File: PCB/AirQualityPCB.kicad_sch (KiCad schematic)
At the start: 28 parts, among them J1 USB_C_Receptacle_USB2.0_16P, J10 SMA-J-P-H-ST-EM1, J2 TestPoint 5V, J3 TestPoint GND, J4 TestPoint 3.3V, U1 Regulator, U13 ESP32-C3-WROOM-02, U2 USBLC6-2SC6, U3 PTS526 SK15 SMTR2 LFS, U4 RFM95WCW

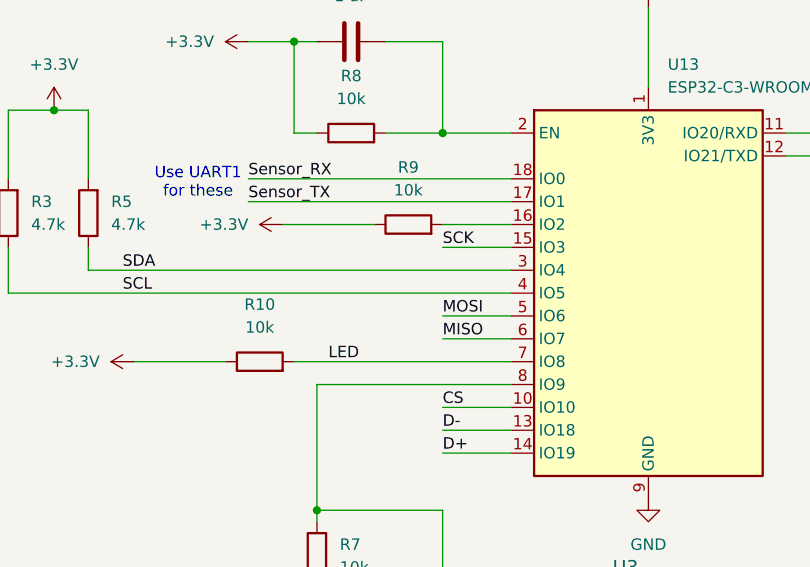
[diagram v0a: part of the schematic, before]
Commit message: Swapped LED to pin 2
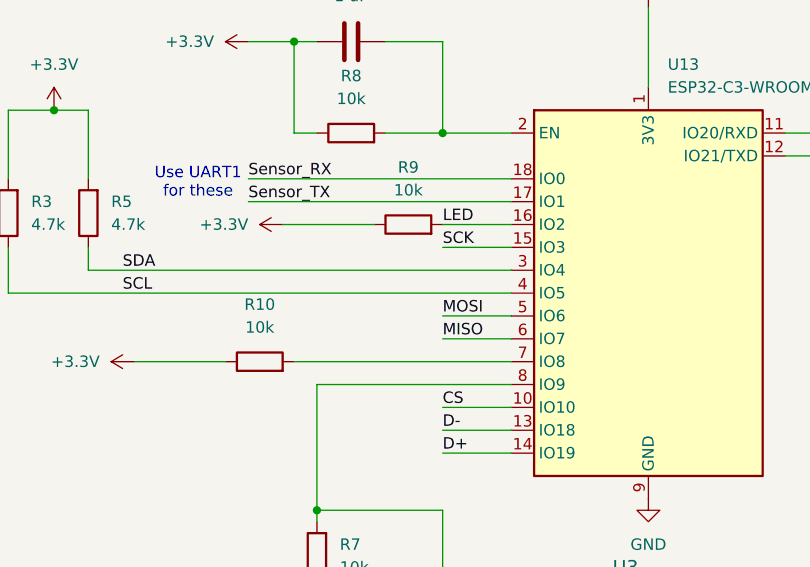
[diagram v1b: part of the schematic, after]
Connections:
- net LED: now also R9.2, U13.16 (IO2); no longer R10.2, U13.7 (IO8)
- new net: R10.2, U13.7 (IO8)
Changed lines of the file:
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@@
+		)
+	)
+	(label "LED"
+		(at 210.8333 60.96 0)
+		(effects
+			(font
+				(size 1.27 1.27)
+			)
+			(justify left bottom)
 		)
 	)
@@
 		(effects
 			(font
-				(size 1.27 1.27)
-			)
-			(justify left bottom)
-		)
-	)
-	(label "LED"
-		(at 198.12 76.2 0)
-		(effects
-			(font

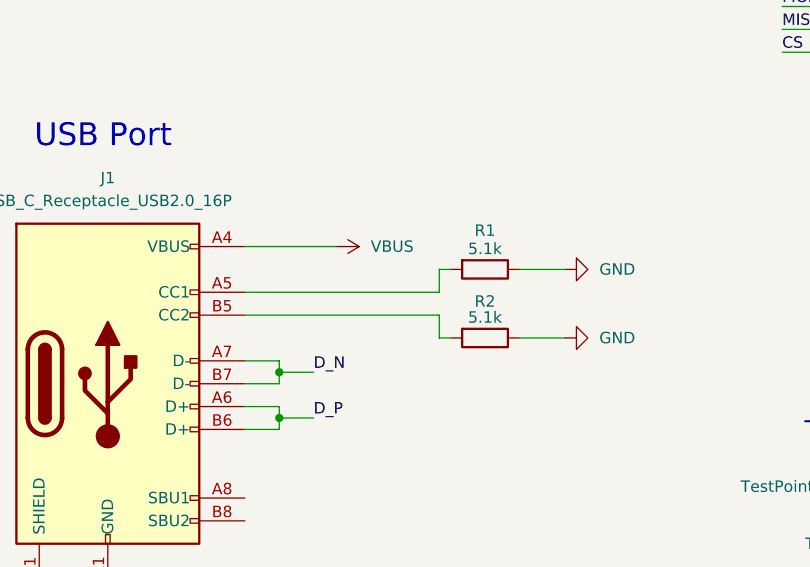
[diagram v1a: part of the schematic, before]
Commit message: Swapped USB CC resistors
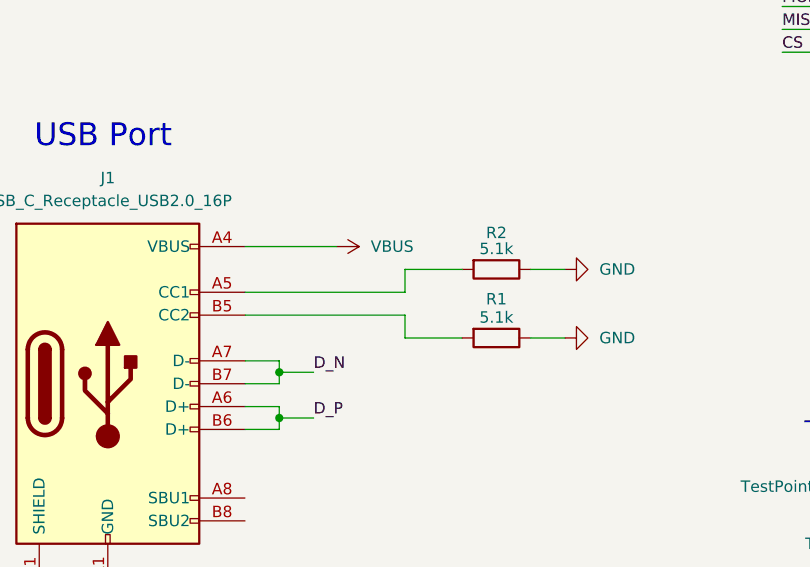
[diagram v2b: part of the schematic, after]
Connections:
- net at R2.2: now also J1.A5 (CC1); no longer J1.B5 (CC2)
- net at R1.2: now also J1.B5 (CC2); no longer J1.A5 (CC1)
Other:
- moved on the sheet: R1, R2
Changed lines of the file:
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@@
 	(title_block
 		(title "AirQualityPCB")
-		(date "2026-03-25")
+		(date "2026-04-13")
 		(rev "1.0")
 		(company "Cornell University")
@@
 	(wire
 		(pts
-			(xy 83.82 144.78) (xy 88.9 144.78)
+			(xy 53.34 139.7) (xy 71.12 139.7)
 		)
 		(stroke
@@
 	(wire
 		(pts
+			(xy 71.12 144.78) (xy 71.12 142.24)
+		)
+		(stroke
+			(width 0)
+			(type default)
+		)
+	)
+	(wire
+		(pts
 			(xy 210.82 83.82) (xy 218.44 83.82)
 		)
@@
 	(wire
 		(pts
+			(xy 77.47 144.78) (xy 71.12 144.78)
+		)
+		(stroke
+			(width 0)
+			(type default)
+		)
+	)
+	(wire
+		(pts
 			(xy 196.85 101.6) (xy 196.85 113.03)
 		)
@@
 	(wire
 		(pts
+			(xy 85.09 137.16) (xy 88.9 137.16)
+		)
+		(stroke
+			(width 0)
+			(type default)
+		)
+	)
+	(wire
+		(pts
 			(xy 50.8 35.56) (xy 58.42 35.56)
 		)
@@
 	(wire
 		(pts
-			(xy 83.82 137.16) (xy 88.9 137.16)
-		)
-		(stroke
-			(width 0)
-			(type default)
-		)
-	)
-	(wire
-		(pts
 			(xy 251.46 109.22) (xy 259.08 109.22)
 		)
@@
 	(wire
 		(pts
-			(xy 74.93 139.7) (xy 53.34 139.7)
-		)
-		(stroke
-			(width 0)
-			(type default)
-		)
-	)
-	(wire
-		(pts
 			(xy 196.85 78.74) (xy 196.85 92.71)
 		)
@@
 	(wire
 		(pts
+			(xy 71.12 142.24) (xy 53.34 142.24)
+		)
+		(stroke
+			(width 0)
+			(type default)
+		)
+	)
+	(wire
+		(pts
 			(xy 53.34 134.62) (xy 63.5 134.62)
 		)
@@
 	(wire
 		(pts
-			(xy 74.93 137.16) (xy 74.93 139.7)
-		)
-		(stroke
-			(width 0)
-			(type default)
-		)
-	)
-	(wire
-		(pts
 			(xy 134.62 134.62) (xy 137.16 134.62)
 		)
@@
 	(wire
 		(pts
+			(xy 71.12 137.16) (xy 77.47 137.16)
+		)
+		(stroke
+			(width 0)
+			(type default)
+		)
+	)
+	(wire
+		(pts
 			(xy 189.23 40.64) (xy 194.31 40.64)
 		)
@@
 	(wire
 		(pts
+			(xy 71.12 137.16) (xy 71.12 139.7)
+		)
+		(stroke
+			(width 0)
+			(type default)
+		)
+	)
+	(wire
+		(pts
 			(xy 194.31 50.8) (xy 194.31 40.64)
 		)
@@
 	(wire
 		(pts
-			(xy 74.93 137.16) (xy 76.2 137.16)
-		)
-		(stroke
-			(width 0)
-			(type default)
-		)
-	)
-	(wire
-		(pts
 			(xy 149.86 118.11) (xy 153.67 118.11)
 		)
@@
 	(wire
 		(pts
+			(xy 85.09 144.78) (xy 88.9 144.78)
+		)
+		(stroke
+			(width 0)
+			(type default)
+		)
+	)
+	(wire
+		(pts
 			(xy 57.15 153.67) (xy 60.96 153.67)
 		)
@@
 	(wire
 		(pts
-			(xy 74.93 144.78) (xy 76.2 144.78)
-		)
-		(stroke
-			(width 0)
-			(type default)
-		)
-	)
-	(wire
-		(pts
 			(xy 210.82 92.71) (xy 210.82 109.22)
 		)
@@
 	(wire
 		(pts
-			(xy 74.93 144.78) (xy 74.93 142.24)
-		)
-		(stroke
-			(width 0)
-			(type default)
-		)
-	)
-	(wire
-		(pts
 			(xy 58.42 35.56) (xy 58.42 38.1)
 		)
@@
 		(pts
 			(xy 27.94 45.72) (xy 27.94 50.8)
-		)
-		(stroke
-			(width 0)
-			(type default)
-		)
-	)
-	(wire
-		(pts
-			(xy 74.93 142.24) (xy 53.34 142.24)
 		)
 		(stroke
@@
 	(symbol
 		(lib_id "Device:R")
-		(at 80.01 144.78 270)
+		(at 81.28 137.16 270)
 		(unit 1)
 		(exclude_from_sim no)
@@
 		(dnp no)
 		(property "Reference" "R2"
-			(at 80.01 140.716 90)
+			(at 81.28 133.096 90)
 			(effects
 				(font
@@
 		)
 		(property "Value" "5.1k"
-			(at 80.01 142.494 90)
+			(at 81.28 134.874 90)
 			(effects
 				(font
@@
 		)
 		(property "Footprint" "Resistor_SMD:R_1206_3216Metric"
-			(at 80.01 143.002 90)
+			(at 81.28 135.382 90)
 			(effects
 				(font
@@
 		)
 		(property "Datasheet" "~"
-			(at 80.01 144.78 0)
+			(at 81.28 137.16 0)
 			(effects
 				(font
@@
 		)
 		(property "Description" "Resistor"
-			(at 80.01 144.78 0)
+			(at 81.28 137.16 0)
 			(effects
 				(font
@@
 		)
 		(property "Manufacturer Part Number" "CRCW12065K10FKEA"
-			(at 80.01 144.78 0)
+			(at 81.28 137.16 0)
 			(effects
 				(font
@@
 	(symbol
 		(lib_id "Device:R")
-		(at 80.01 137.16 270)
+		(at 81.28 144.78 270)
 		(unit 1)
 		(exclude_from_sim no)
@@
 		(dnp no)
 		(property "Reference" "R1"
-			(at 80.01 132.842 90)
+			(at 81.28 140.462 90)
 			(effects
 				(font
@@
 		)
 		(property "Value" "5.1k"
-			(at 80.01 134.874 90)
+			(at 81.28 142.494 90)
 			(effects
 				(font
@@
 		)
 		(property "Footprint" "Resistor_SMD:R_1206_3216Metric"
-			(at 80.01 135.382 90)
+			(at 81.28 143.002 90)
 			(effects
 				(font
@@
 		)
 		(property "Datasheet" "~"
-			(at 80.01 137.16 0)
+			(at 81.28 144.78 0)
 			(effects
 				(font
@@
 		)
 		(property "Description" "Resistor"
-			(at 80.01 137.16 0)
+			(at 81.28 144.78 0)
 			(effects
 				(font
@@
 		)
 		(property "Manufacturer Part Number" "CRCW12065K10FKEA"
-			(at 80.01 137.16 0)
-			(effects
-				(font
+			(at 81.28 144.78 0)
+			(effects
+				(font
